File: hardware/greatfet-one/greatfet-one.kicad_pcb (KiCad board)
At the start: 4 copper layers, 70.6 x 53.3 mm, 91 parts, among them J1 NEIGHBOR1, J2 NEIGHBOR2, J3 USB-MICRO-B-SHIELDED, J4 USB-MICRO-B-SHIELDED, J5 JTAG, J7 BONUS_ROW, SW1 DFU, SW2 RESET, U1 LPC4330FBD144, U2 W25Q16DV, U3 AP7333, U4 IP4220CZ6, U5 AP2553W6-7, X1 MCU_XTAL, X2 RTC_XTAL

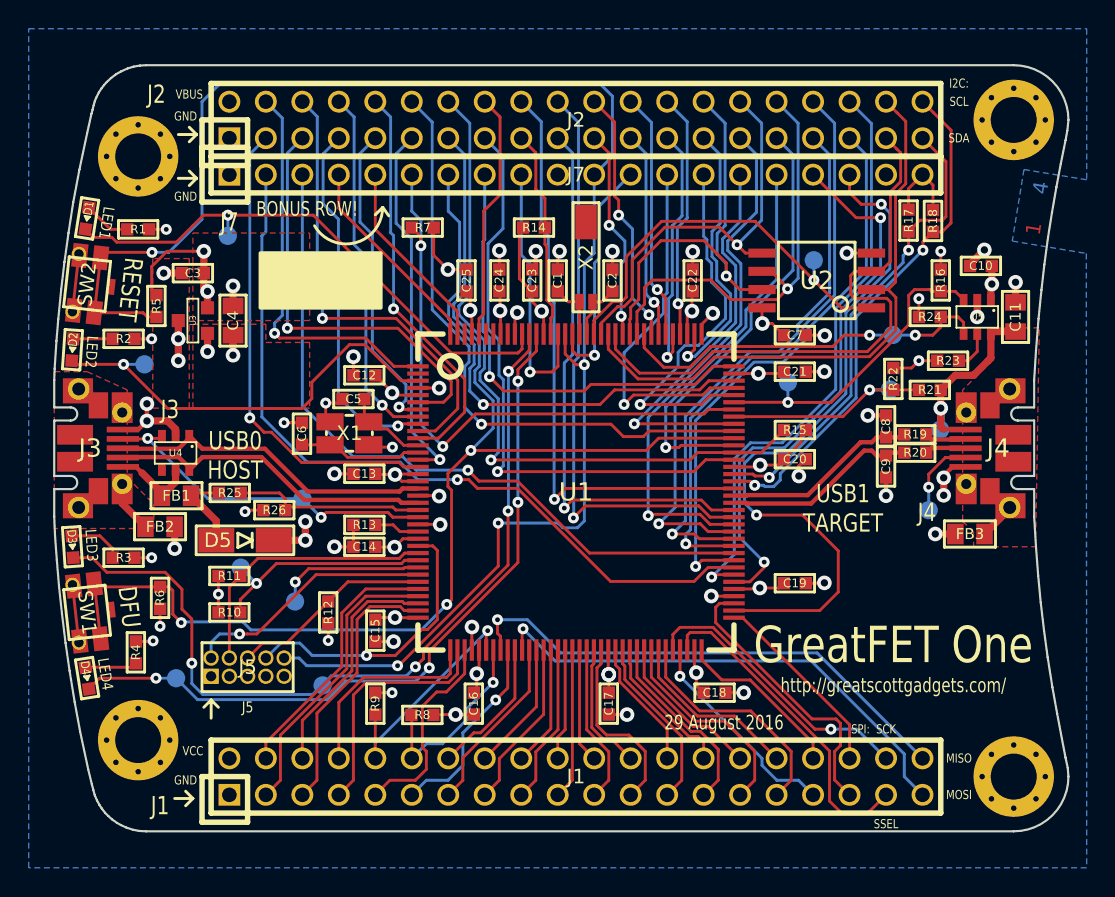
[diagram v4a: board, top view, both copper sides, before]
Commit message: GreatFET One: spread a few components apart for easier hand assembly
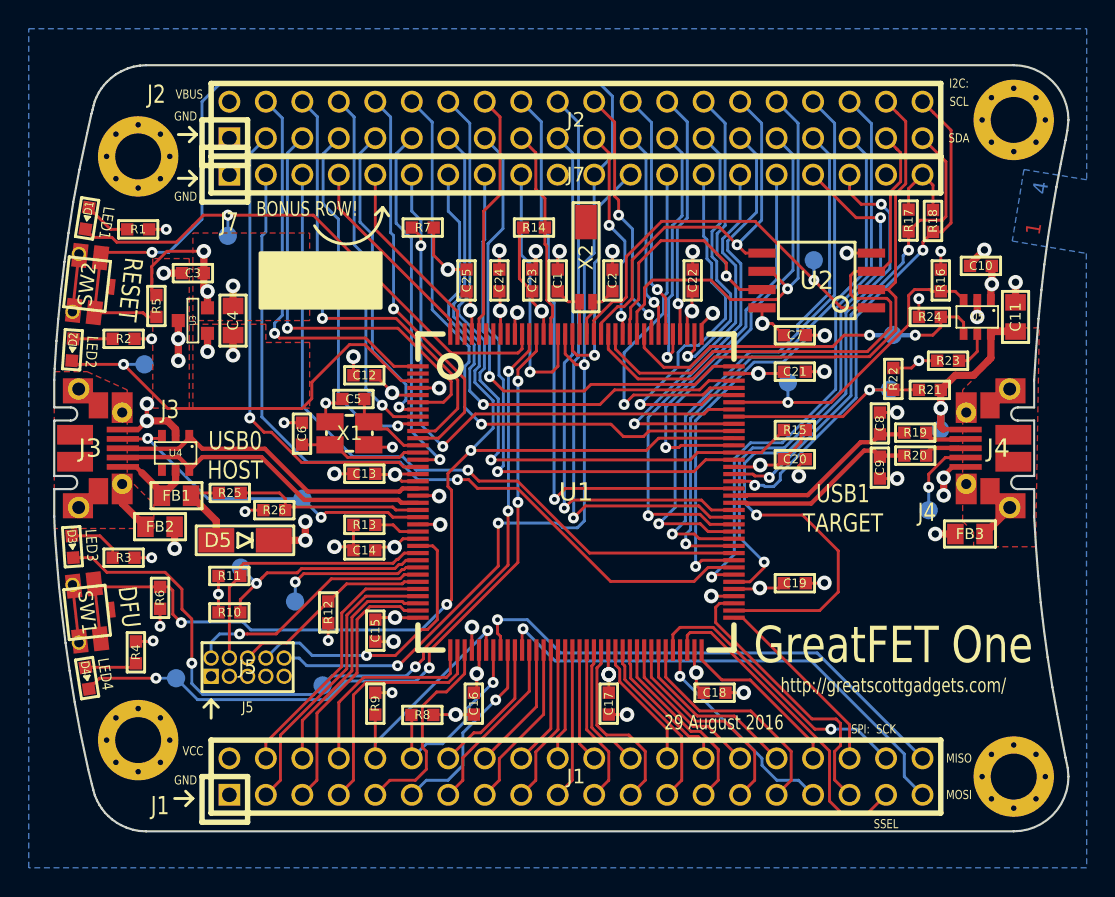
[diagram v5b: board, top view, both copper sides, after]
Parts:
- moved C8 0.48 mm to (163.4, 96.1)
- moved C9 0.44 mm to (163.4, 99.1)
- moved C14 0.25 mm to (127.5, 104.9)
- moved R20 0.21 mm to (165.9, 98.3)
- moved R19 0.12 mm to (165.9, 96.7)

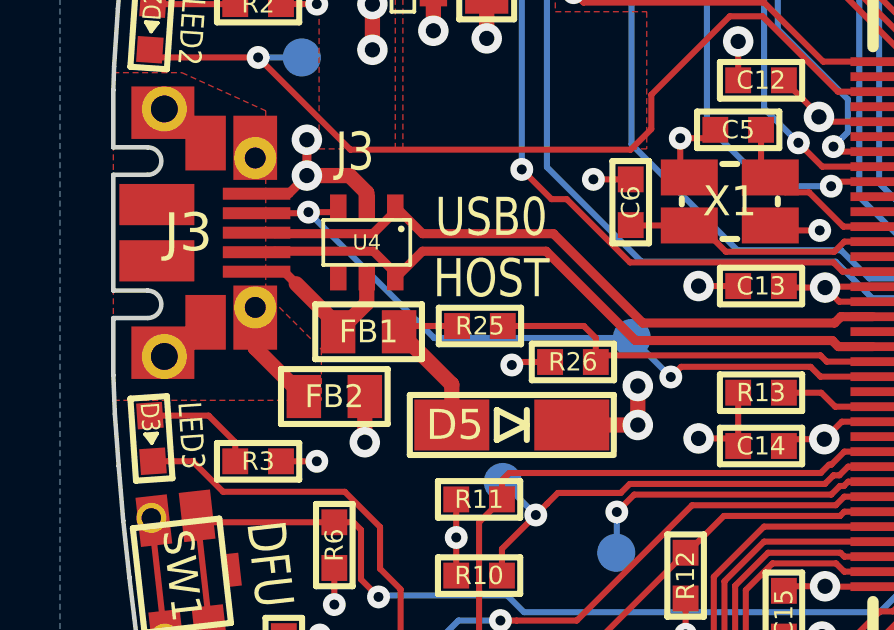
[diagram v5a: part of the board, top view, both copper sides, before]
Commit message: GreatFET One: more USB0 test points
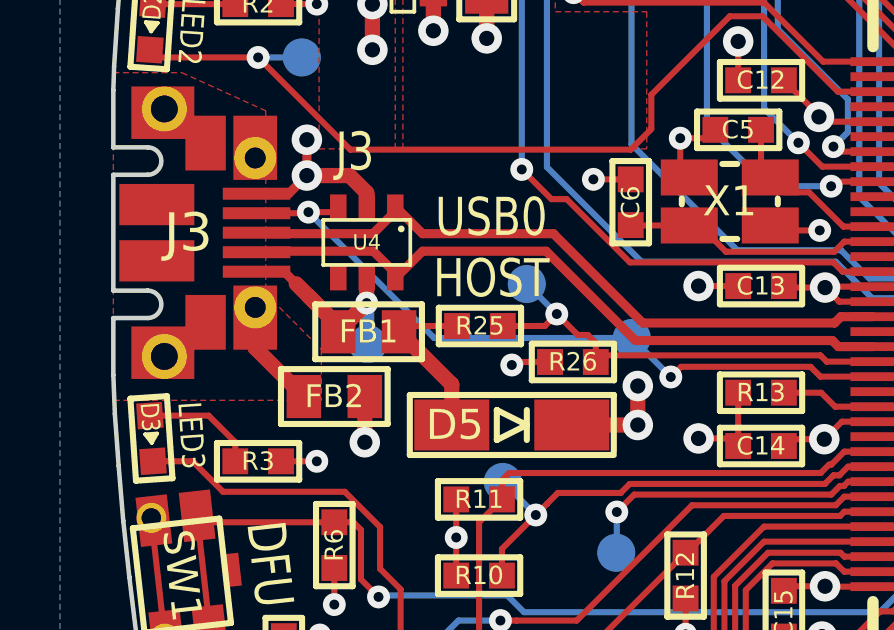
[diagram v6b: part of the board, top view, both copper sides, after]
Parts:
- added TP14: USB0_VBUS, gsg-modules:TESTPOINT-50MIL, B.Cu at (114.4, 101.5)
- added TP15: USB0_SENSE, gsg-modules:TESTPOINT-50MIL, B.Cu at (119.7, 99.5)
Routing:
- net /USB0_VBUS: track 5.84 -> 9.74 mm, vias 0 -> 1
- net /USB0_SENSE: track 13.5 -> 15.1 mm, vias 0 -> 1
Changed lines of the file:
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@@
 (kicad_pcb (version 4) (host pcbnew "(2015-08-18 BZR 6102)-product")
   (general
-    (links 356)
+    (links 358)
     (no_connects 0)
-    (area 93.271704 68.58 207.466001 199.465001)
+    (area 105.842999 71.044999 176.605001 124.535001)
     (thickness 1.6)
     (drawings 154)
-    (tracks 1482)
+    (tracks 1495)
     (zones 0)
-    (modules 91)
+    (modules 93)
     (nets 141)
   )
@@
   )
   (setup
-    (last_trace_width 0.3048)
+    (last_trace_width 0.2032)
     (user_trace_width 0.3048)
     (user_trace_width 0.508)
@@
       (net 1 GND) (solder_mask_margin 0.1016) (clearance 0.1778))
   )
+  (module gsg-modules:TESTPOINT-50MIL (layer B.Cu)
+    (at 114.4 101.5)
+    (fp_text reference TP14 (at 0 0) (layer B.SilkS)
+      (effects (font (size 0.381 0.381) (thickness 0.09652)) (justify mirror))
+    )
+    (fp_text value USB0_VBUS (at 0 0) (layer B.SilkS) hide
+      (effects (font (size 0.508 0.508) (thickness 0.127)) (justify mirror))
+    )
+    (fp_circle (center 0 0) (end 0.7112 0) (layer B.SilkS) (width 0.2032))
+    (pad 1 smd circle (at 0 0) (size 1.27 1.27) (layers B.Cu B.Mask)
+      (net 139 /USB0_VBUS))
+  )
+  (module gsg-modules:TESTPOINT-50MIL (layer B.Cu)
+    (at 119.7 99.5)
+    (fp_text reference TP15 (at 0 0) (layer B.SilkS)
+      (effects (font (size 0.381 0.381) (thickness 0.09652)) (justify mirror))
+    )
+    (fp_text value USB0_SENSE (at 0 0) (layer B.SilkS) hide
+      (effects (font (size 0.508 0.508) (thickness 0.127)) (justify mirror))
+    )
+    (fp_circle (center 0 0) (end 0.7112 0) (layer B.SilkS) (width 0.2032))
+    (pad 1 smd circle (at 0 0) (size 1.27 1.27) (layers B.Cu B.Mask)
+      (net 140 /USB0_SENSE))
+  )
   (gr_line (start 116.84 115.316) (end 116.84 116.586) (angle 90) (layer F.SilkS) (width 0.2032))
   (gr_line (start 116.84 115.316) (end 117.348 115.824) (angle 90) (layer F.SilkS) (width 0.2032))
@@
   (segment (start 117.376 100.9) (end 115.635 100.9) (width 0.2032) (layer F.Cu) (net 138))
   (segment (start 115.635 100.9) (end 115.443 101.092) (width 0.2032) (layer F.Cu) (net 138))
+  (segment (start 114.361618 100.134949) (end 114.361618 101.461618) (width 0.508) (layer B.Cu) (net 139))
+  (segment (start 114.361618 101.461618) (end 114.4 101.5) (width 0.508) (layer B.Cu) (net 139))
+  (segment (start 112.441994 99.919794) (end 112.014 99.4918) (width 0.508) (layer F.Cu) (net 139))
+  (segment (start 113.411 100.8888) (end 112.441994 99.919794) (width 0.508) (layer F.Cu) (net 139))
+  (segment (start 114.366 100.137) (end 114.361618 100.134949) (width 0.508) (layer F.Cu) (net 139))
+  (segment (start 114.361618 100.134949) (end 114.366 99.314) (width 0.508) (layer F.Cu) (net 139))
+  (segment (start 113.275111 100.752911) (end 113.743656 100.752911) (width 0.508) (layer F.Cu) (net 139))
+  (via (at 114.361618 100.134949) (size 0.762) (drill 0.3302) (layers F.Cu B.Cu) (net 139))
+  (segment (start 112.441994 99.919794) (end 113.275111 100.752911) (width 0.508) (layer F.Cu) (net 139))
+  (segment (start 113.743656 100.752911) (end 114.361618 100.134949) (width 0.508) (layer F.Cu) (net 139))
   (segment (start 113.411 100.8888) (end 113.411 101.092) (width 0.508) (layer F.Cu) (net 139))
-  (segment (start 113.411 100.8888) (end 112.014 99.4918) (width 0.508) (layer F.Cu) (net 139))
   (segment (start 112.014 99.4918) (end 111.6122 99.09) (width 0.3048) (layer F.Cu) (net 139))
   (segment (start 110.693 99.09) (end 111.6122 99.09) (width 0.3048) (layer F.Cu) (net 139))
   (segment (start 113.411 101.092) (end 114.366 100.137) (width 0.508) (layer F.Cu) (net 139))
-  (segment (start 114.366 100.137) (end 114.366 99.314) (width 0.508) (layer F.Cu) (net 139))
+  (segment (start 120.7 100.5) (end 119.7 99.5) (width 0.2032) (layer B.Cu) (net 140))
+  (segment (start 121.735 101.2) (end 121.4 101.2) (width 0.2032) (layer F.Cu) (net 140))
+  (segment (start 121.4 101.2) (end 120.7 100.5) (width 0.2032) (layer F.Cu) (net 140))
+  (segment (start 122 102.1) (end 122 101.465) (width 0.2032) (layer F.Cu) (net 140))
+  (segment (start 122 101.465) (end 121.735 101.2) (width 0.2032) (layer F.Cu) (net 140))
+  (segment (start 118.9 100.9) (end 120.3 100.9) (width 0.2032) (layer F.Cu) (net 140))
+  (segment (start 120.3 100.9) (end 120.7 100.5) (width 0.2032) (layer F.Cu) (net 140))
+  (via (at 120.7 100.5) (size 0.762) (drill 0.3302) (layers F.Cu B.Cu) (net 140))
   (segment (start 122.2206 101.8794) (end 122 102.1) (width 0.2032) (layer F.Cu) (net 140))
-  (segment (start 118.9 100.9) (end 121.6 100.9) (width 0.2032) (layer F.Cu) (net 140))
-  (segment (start 122 101.3) (end 122 102.1) (width 0.2032) (layer F.Cu) (net 140))
-  (segment (start 121.6 100.9) (end 122 101.3) (width 0.2032) (layer F.Cu) (net 140))
   (segment (start 122.2206 101.8794) (end 129.4892 101.8794) (width 0.2032) (layer F.Cu) (net 140))
   (segment (start 129.69748 102.08768) (end 131.23926 102.08768) (width 0.2032) (layer F.Cu) (net 140))

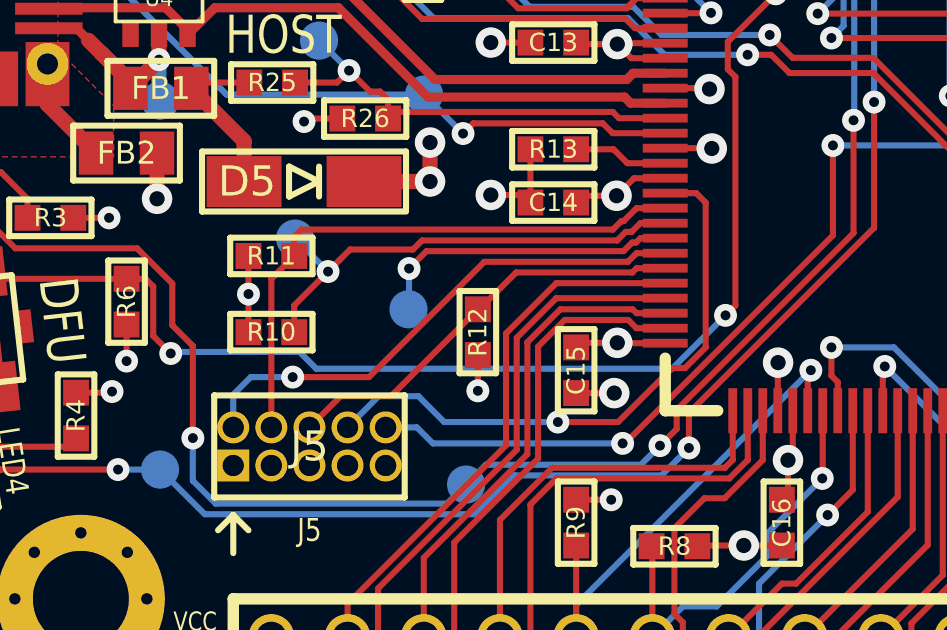
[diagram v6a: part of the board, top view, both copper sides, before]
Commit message: GreatFET One: more JTAG test points
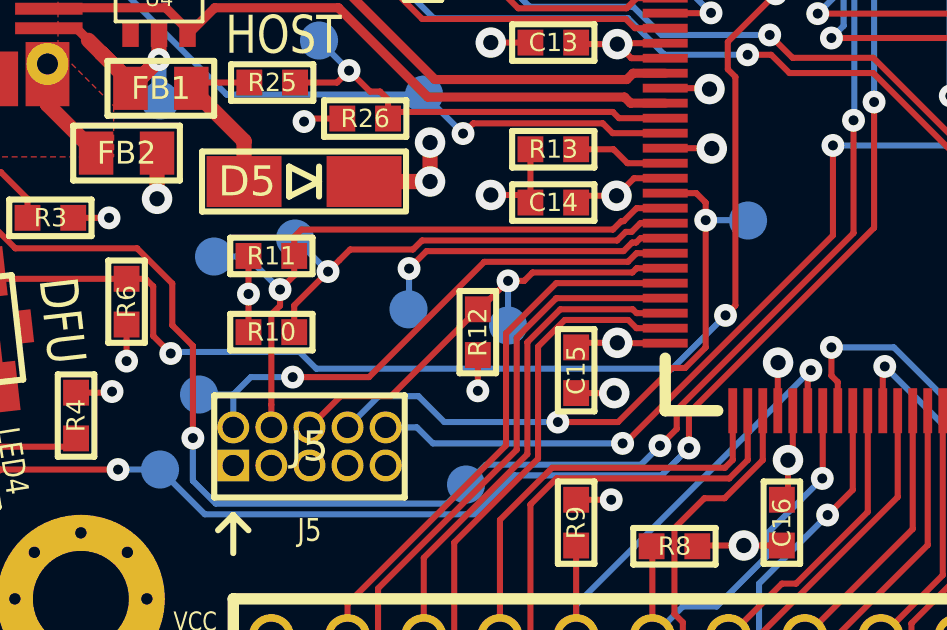
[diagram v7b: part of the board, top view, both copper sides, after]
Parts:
- added TP16: TMS, gsg-modules:TESTPOINT-50MIL, B.Cu at (115.7, 111.3)
- added TP17: TCK, gsg-modules:TESTPOINT-50MIL, B.Cu at (116.2, 106.7)
- added TP18: TDO, gsg-modules:TESTPOINT-50MIL, B.Cu at (126.0, 109.0)
- added TP19: TDI, gsg-modules:TESTPOINT-50MIL, B.Cu at (134.0, 105.5)
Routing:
- net /TCK: track 19.4 -> 22.1 mm, vias 0 -> 1
- net /TDO: track 14.1 -> 15.6 mm, vias 0 -> 1
- net /TDI: track 20.1 -> 21.5 mm, vias 1 -> 2
- net /TMS: track 17.4 -> 18.6 mm
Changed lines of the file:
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@@
 (kicad_pcb (version 4) (host pcbnew "(2015-08-18 BZR 6102)-product")
   (general
-    (links 358)
+    (links 362)
     (no_connects 0)
     (area 105.842999 71.044999 176.605001 124.535001)
     (thickness 1.6)
     (drawings 154)
-    (tracks 1495)
+    (tracks 1513)
     (zones 0)
-    (modules 93)
+    (modules 97)
     (nets 141)
   )
@@
       (net 140 /USB0_SENSE))
   )
+  (module gsg-modules:TESTPOINT-50MIL (layer B.Cu)
+    (at 115.7 111.3)
+    (fp_text reference TP16 (at 0 0) (layer B.SilkS)
+      (effects (font (size 0.381 0.381) (thickness 0.09652)) (justify mirror))
+    )
+    (fp_text value TMS (at 0 0) (layer B.SilkS) hide
+      (effects (font (size 0.508 0.508) (thickness 0.127)) (justify mirror))
+    )
+    (fp_circle (center 0 0) (end 0.7112 0) (layer B.SilkS) (width 0.2032))
+    (pad 1 smd circle (at 0 0) (size 1.27 1.27) (layers B.Cu B.Mask)
+      (net 96 /TMS))
+  )
+  (module gsg-modules:TESTPOINT-50MIL (layer B.Cu)
+    (at 116.2 106.7)
+    (fp_text reference TP17 (at 0 0) (layer B.SilkS)
+      (effects (font (size 0.381 0.381) (thickness 0.09652)) (justify mirror))
+    )
+    (fp_text value TCK (at 0 0) (layer B.SilkS) hide
+      (effects (font (size 0.508 0.508) (thickness 0.127)) (justify mirror))
+    )
+    (fp_circle (center 0 0) (end 0.7112 0) (layer B.SilkS) (width 0.2032))
+    (pad 1 smd circle (at 0 0) (size 1.27 1.27) (layers B.Cu B.Mask)
+      (net 97 /TCK))
+  )
+  (module gsg-modules:TESTPOINT-50MIL (layer B.Cu)
+    (at 126 109)
+    (fp_text reference TP18 (at 0 0) (layer B.SilkS)
+      (effects (font (size 0.381 0.381) (thickness 0.09652)) (justify mirror))
+    )
+    (fp_text value TDO (at 0 0) (layer B.SilkS) hide
+      (effects (font (size 0.508 0.508) (thickness 0.127)) (justify mirror))
+    )
+    (fp_circle (center 0 0) (end 0.7112 0) (layer B.SilkS) (width 0.2032))
+    (pad 1 smd circle (at 0 0) (size 1.27 1.27) (layers B.Cu B.Mask)
+      (net 98 /TDO))
+  )
+  (module gsg-modules:TESTPOINT-50MIL (layer B.Cu)
+    (at 134 105.5)
+    (fp_text reference TP19 (at 0 0) (layer B.SilkS)
+      (effects (font (size 0.381 0.381) (thickness 0.09652)) (justify mirror))
+    )
+    (fp_text value TDI (at 0 0) (layer B.SilkS) hide
+      (effects (font (size 0.508 0.508) (thickness 0.127)) (justify mirror))
+    )
+    (fp_circle (center 0 0) (end 0.7112 0) (layer B.SilkS) (width 0.2032))
+    (pad 1 smd circle (at 0 0) (size 1.27 1.27) (layers B.Cu B.Mask)
+      (net 100 /TDI))
+  )
   (gr_line (start 116.84 115.316) (end 116.84 116.586) (angle 90) (layer F.SilkS) (width 0.2032))
   (gr_line (start 116.84 115.316) (end 117.348 115.824) (angle 90) (layer F.SilkS) (width 0.2032))
@@
   (segment (start 168.874758 97.1804) (end 168.915158 97.14) (width 0.3048) (layer F.Cu) (net 95))
   (segment (start 168.915158 97.14) (end 170.1174 97.14) (width 0.3048) (layer F.Cu) (net 95) (status 20))
+  (segment (start 116.84 111.3028) (end 116.8372 111.3) (width 0.2032) (layer B.Cu) (net 96))
+  (segment (start 116.8372 111.3) (end 115.7 111.3) (width 0.2032) (layer B.Cu) (net 96))
   (segment (start 129.995962 106.87556) (end 125.209318 106.87556) (width 0.2032) (layer F.Cu) (net 96))
   (segment (start 125.209318 106.87556) (end 121.366278 110.7186) (width 0.2032) (layer F.Cu) (net 96))
@@
   (segment (start 118.8212 110.7186) (end 117.4242 110.7186) (width 0.2032) (layer B.Cu) (net 96))
   (via (at 118.8212 110.7186) (size 0.762) (drill 0.3302) (layers F.Cu B.Cu) (net 96))
+  (segment (start 118.4 107.8) (end 118.4 108.338815) (width 0.2032) (layer F.Cu) (net 97))
+  (segment (start 118.4 108.338815) (end 118.11 108.628815) (width 0.2032) (layer F.Cu) (net 97))
+  (segment (start 118.11 108.628815) (end 118.11 111.640659) (width 0.2032) (layer F.Cu) (net 97))
+  (segment (start 118.11 111.640659) (end 118.11 112.395) (width 0.2032) (layer F.Cu) (net 97))
+  (segment (start 118.4 107.8) (end 117.3 106.7) (width 0.2032) (layer B.Cu) (net 97))
+  (segment (start 117.3 106.7) (end 116.2 106.7) (width 0.2032) (layer B.Cu) (net 97))
+  (segment (start 118.872 106.68) (end 118.872 107.328) (width 0.2032) (layer F.Cu) (net 97))
+  (segment (start 118.872 107.328) (end 118.4 107.8) (width 0.2032) (layer F.Cu) (net 97))
+  (via (at 118.4 107.8) (size 0.762) (drill 0.3302) (layers F.Cu B.Cu) (net 97))
   (segment (start 131.23926 105.08742) (end 130.28549 105.08742) (width 0.2032) (layer F.Cu) (net 97))
   (segment (start 130.28549 105.08742) (end 129.851177 105.521733) (width 0.2032) (layer F.Cu) (net 97))
@@
   (segment (start 129.497092 105.8) (end 119.117 105.8) (width 0.2032) (layer F.Cu) (net 97))
   (segment (start 118.872 106.045) (end 118.872 106.68) (width 0.2032) (layer F.Cu) (net 97))
-  (segment (start 118.872 106.68) (end 118.11 107.442) (width 0.2032) (layer F.Cu) (net 97))
-  (segment (start 118.11 107.442) (end 118.11 112.395) (width 0.2032) (layer F.Cu) (net 97))
+  (segment (start 130.14326 107.23117) (end 126.818215 107.23117) (width 0.2032) (layer F.Cu) (net 98))
+  (segment (start 126.818215 107.23117) (end 126.538815 107.51057) (width 0.2032) (layer F.Cu) (net 98))
+  (segment (start 126.538815 107.51057) (end 126 107.51057) (width 0.2032) (layer F.Cu) (net 98))
+  (segment (start 126 107.51057) (end 126 109) (width 0.2032) (layer B.Cu) (net 98))
+  (segment (start 124.9934 108.458) (end 125.05257 108.458) (width 0.2032) (layer F.Cu) (net 98))
+  (segment (start 125.05257 108.458) (end 126 107.51057) (width 0.2032) (layer F.Cu) (net 98))
+  (via (at 126 107.51057) (size 0.762) (drill 0.3302) (layers F.Cu B.Cu) (net 98))
   (segment (start 131.23926 107.08894) (end 130.28549 107.08894) (width 0.2032) (layer F.Cu) (net 98))
   (segment (start 130.28549 107.08894) (end 130.14326 107.23117) (width 0.2032) (layer F.Cu) (net 98))
-  (segment (start 130.14326 107.23117) (end 126.26883 107.23117) (width 0.2032) (layer F.Cu) (net 98))
-  (segment (start 126.26883 107.23117) (end 125.042 108.458) (width 0.2032) (layer F.Cu) (net 98))
   (segment (start 125.042 108.458) (end 124.9934 108.458) (width 0.2032) (layer F.Cu) (net 98))
   (segment (start 124.9934 108.458) (end 122.0978 111.3536) (width 0.2032) (layer F.Cu) (net 98) (status 10))
   (segment (start 120.4214 111.3536) (end 119.38 112.395) (width 0.2032) (layer F.Cu) (net 98) (status 20))
   (segment (start 122.0978 111.3536) (end 120.4214 111.3536) (width 0.2032) (layer F.Cu) (net 98))
+  (segment (start 132.588 105.488206) (end 133.988206 105.488206) (width 0.2032) (layer B.Cu) (net 100))
+  (segment (start 133.988206 105.488206) (end 134 105.5) (width 0.2032) (layer B.Cu) (net 100))
+  (segment (start 132.588 105.488206) (end 132.588 109.728) (width 0.2032) (layer F.Cu) (net 100))
+  (segment (start 132.588 104.902) (end 132.588 105.488206) (width 0.2032) (layer F.Cu) (net 100))
+  (via (at 132.588 105.488206) (size 0.762) (drill 0.3302) (layers F.Cu B.Cu) (net 100))
   (segment (start 123.0122 111.3536) (end 121.6914 111.3536) (width 0.2032) (layer B.Cu) (net 100))
   (segment (start 121.6914 111.3536) (end 120.65 112.395) (width 0.2032) (layer B.Cu) (net 100) (status 20))
@@
   (segment (start 131.9022 110.4138) (end 131.4704 110.4138) (width 0.2032) (layer F.Cu) (net 100))
   (segment (start 132.588 109.728) (end 131.9022 110.4138) (width 0.2032) (layer F.Cu) (net 100))
-  (segment (start 132.588 104.902) (end 132.588 109.728) (width 0.2032) (layer F.Cu) (net 100))
   (segment (start 132.27304 104.58704) (end 132.588 104.902) (width 0.2032) (layer F.Cu) (net 100))
   (segment (start 131.23926 104.58704) (end 132.27304 104.58704) (width 0.2032) (layer F.Cu) (net 100) (status 10))
